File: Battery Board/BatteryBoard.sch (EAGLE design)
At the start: 19 parts, among them IC1 MCP73831T-2ATI_OT, IC2 STM809TWX6F, J0 1725656, U0 STM32L031K4U6, U1 IAUC60N04S6L030HATMA1

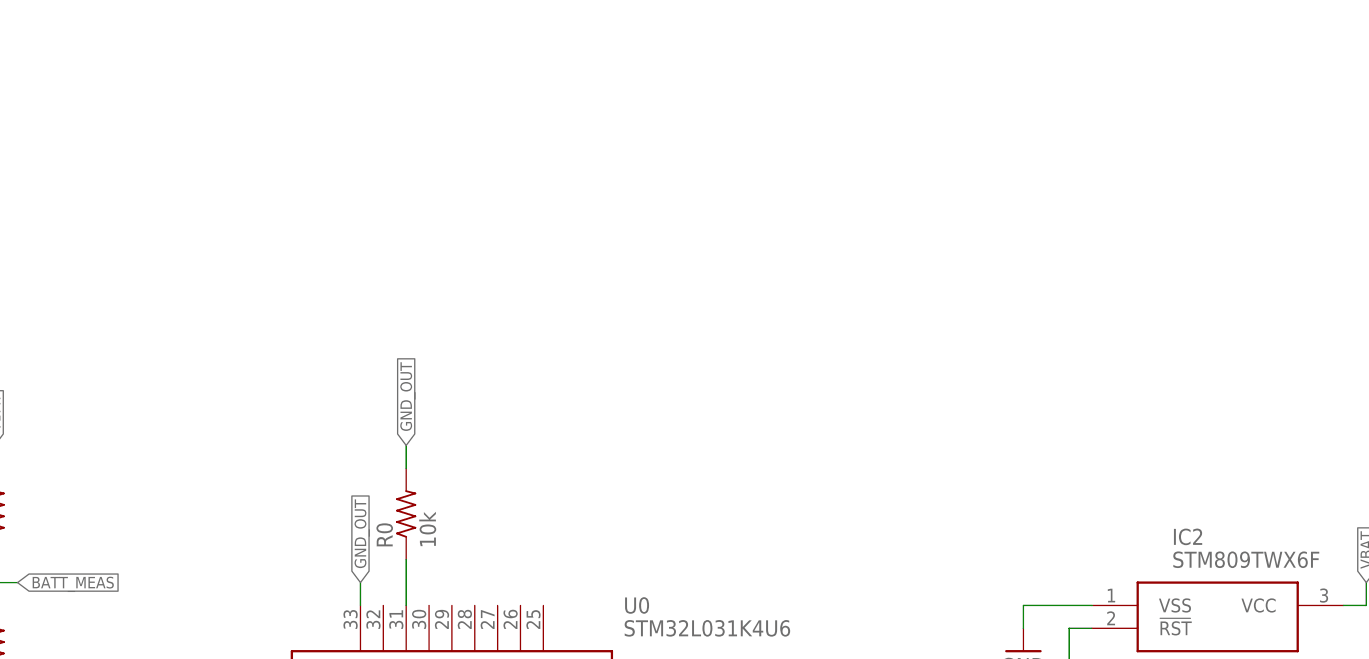
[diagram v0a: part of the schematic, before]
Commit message: Buck Converter Obtained (Switching frequency not)
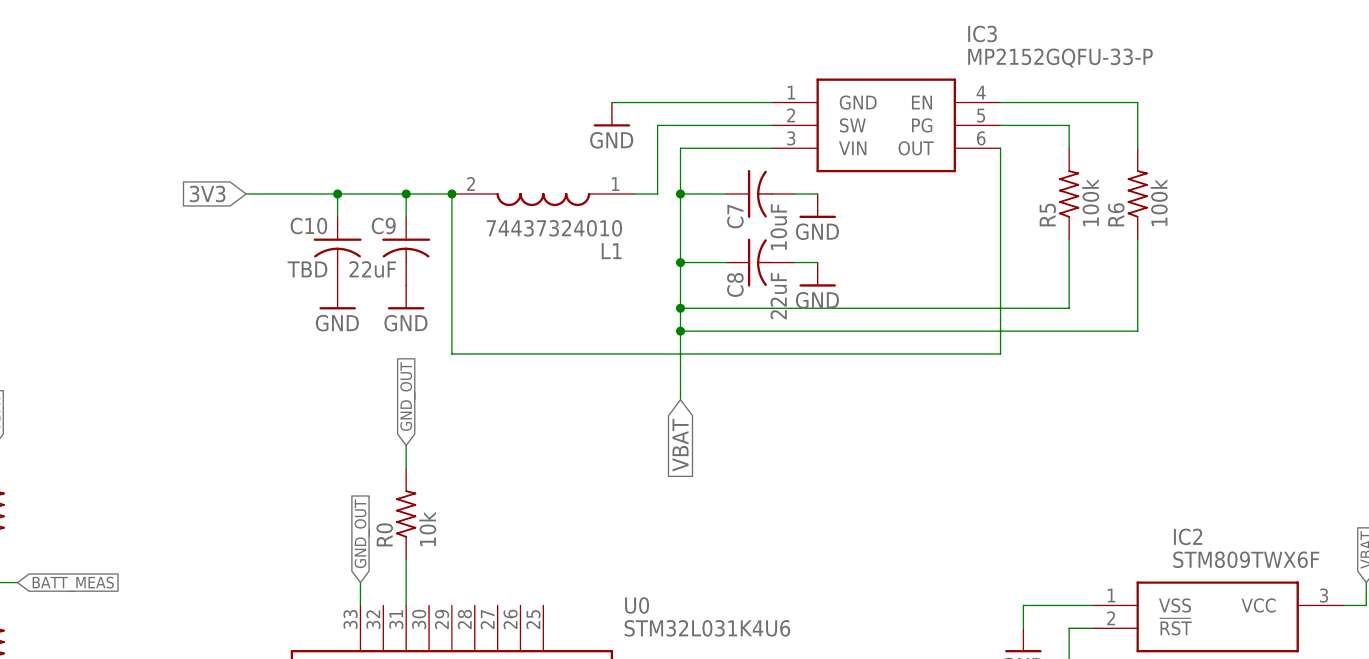
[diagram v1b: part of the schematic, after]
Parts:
- added C10: TBD, rcl:C-USC0805
- added C7: 10uF, rcl:C-USC0805
- added C8, C9: 22uF, rcl:C-USC0805
- added IC3: MP2152GQFU-33-P, SamacSys_Parts:MP2152GQFU-33-P
- added L1: 74437324010, SamacSys_Parts:74437324010
- added R5, R6: 100k, rcl:R-US_R0805
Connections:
- new net N$5: IC3.PG, R5.2
- new net N$6: IC3.EN, R6.2
- new net N$7: IC3.SW, L1.1
- net 3V3: now also C10.1, C9.1, IC3.OUT, L1.2
- net GND: now also C10.2, C7.2, C8.2, C9.2, IC3.GND
- net VBAT: now also C7.1, C8.1, IC3.VIN, R5.1, R6.1
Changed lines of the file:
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@@
 <part name="GND11" library="supply1" library_urn="urn:adsk.eagle:library:371" deviceset="GND" device=""/>
 <part name="U1" library="MarkParts" deviceset="IAUC60N04S6L030HATMA1" device=""/>
+<part name="IC3" library="SamacSys_Parts" deviceset="MP2152GQFU-33-P" device=""/>
+<part name="GND1" library="supply1" library_urn="urn:adsk.eagle:library:371" deviceset="GND" device=""/>
+<part name="R5" library="rcl" library_urn="urn:adsk.eagle:library:334" deviceset="R-US_" device="R0805" package3d_urn="urn:adsk.eagle:package:23553/2" value="100k"/>
+<part name="R6" library="rcl" library_urn="urn:adsk.eagle:library:334" deviceset="R-US_" device="R0805" package3d_urn="urn:adsk.eagle:package:23553/2" value="100k"/>
+<part name="C7" library="rcl" library_urn="urn:adsk.eagle:library:334" deviceset="C-US" device="C0805" package3d_urn="urn:adsk.eagle:package:23617/2" value="10uF"/>
+<part name="C8" library="rcl" library_urn="urn:adsk.eagle:library:334" deviceset="C-US" device="C0805" package3d_urn="urn:adsk.eagle:package:23617/2" value="22uF"/>
+<part name="GND4" library="supply1" library_urn="urn:adsk.eagle:library:371" deviceset="GND" device=""/>
+<part name="GND13" library="supply1" library_urn="urn:adsk.eagle:library:371" deviceset="GND" device=""/>
+<part name="L1" library="SamacSys_Parts" deviceset="74437324010" device=""/>
+<part name="C9" library="rcl" library_urn="urn:adsk.eagle:library:334" deviceset="C-US" device="C0805" package3d_urn="urn:adsk.eagle:package:23617/2" value="22uF"/>
+<part name="C10" library="rcl" library_urn="urn:adsk.eagle:library:334" deviceset="C-US" device="C0805" package3d_urn="urn:adsk.eagle:package:23617/2" value="TBD"/>
+<part name="GND14" library="supply1" library_urn="urn:adsk.eagle:library:371" deviceset="GND" device=""/>
+<part name="GND15" library="supply1" library_urn="urn:adsk.eagle:library:371" deviceset="GND" device=""/>
 </parts>
 <sheets>
@@
 <attribute name="VALUE" x="131.8006" y="57.3786" size="2.0828" layer="96" ratio="6" rot="SR0"/>
 </instance>
+<instance part="IC3" gate="G$1" x="73.66" y="124.46" smashed="yes">
+<attribute name="NAME" x="95.25" y="132.08" size="1.778" layer="95" align="center-left"/>
+<attribute name="VALUE" x="95.25" y="129.54" size="1.778" layer="96" align="center-left"/>
+</instance>
+<instance part="GND1" gate="1" x="55.88" y="121.92" smashed="yes">
+<attribute name="VALUE" x="53.34" y="119.38" size="1.778" layer="96"/>
+</instance>
+<instance part="R5" gate="G$1" x="106.68" y="114.3" smashed="yes" rot="R90">
+<attribute name="NAME" x="105.1814" y="110.49" size="1.778" layer="95" rot="R90"/>
+<attribute name="VALUE" x="109.982" y="110.49" size="1.778" layer="96" rot="R90"/>
+</instance>
+<instance part="R6" gate="G$1" x="114.3" y="114.3" smashed="yes" rot="R90">
+<attribute name="NAME" x="112.8014" y="110.49" size="1.778" layer="95" rot="R90"/>
+<attribute name="VALUE" x="117.602" y="110.49" size="1.778" layer="96" rot="R90"/>
+</instance>
+<instance part="C7" gate="G$1" x="71.12" y="114.3" smashed="yes" rot="MR270">
+<attribute name="NAME" x="70.485" y="113.284" size="1.778" layer="95" rot="MR270"/>
+<attribute name="VALUE" x="75.311" y="113.284" size="1.778" layer="96" rot="MR270"/>
+</instance>
+<instance part="C8" gate="G$1" x="71.12" y="106.68" smashed="yes" rot="MR270">
+<attribute name="NAME" x="70.485" y="105.664" size="1.778" layer="95" rot="MR270"/>
+<attribute name="VALUE" x="75.311" y="105.664" size="1.778" layer="96" rot="MR270"/>
+</instance>
+<instance part="GND4" gate="1" x="78.74" y="111.76" smashed="yes">
+<attribute name="VALUE" x="76.2" y="109.22" size="1.778" layer="96"/>
+</instance>
+<instance part="GND13" gate="1" x="78.74" y="104.14" smashed="yes">
+<attribute name="VALUE" x="76.2" y="101.6" size="1.778" layer="96"/>
+</instance>
+<instance part="L1" gate="G$1" x="58.42" y="114.3" smashed="yes" rot="R180">
+<attribute name="NAME" x="57.15" y="107.95" size="1.778" layer="95" rot="R180" align="center-left"/>
+<attribute name="VALUE" x="57.15" y="110.49" size="1.778" layer="96" rot="R180" align="center-left"/>
+</instance>
+<instance part="C9" gate="G$1" x="33.02" y="109.22" smashed="yes" rot="MR0">
+<attribute name="NAME" x="32.004" y="109.855" size="1.778" layer="95" rot="MR0"/>
+<attribute name="VALUE" x="32.004" y="105.029" size="1.778" layer="96" rot="MR0"/>
+</instance>
+<instance part="C10" gate="G$1" x="25.4" y="109.22" smashed="yes" rot="MR0">
+<attribute name="NAME" x="24.384" y="109.855" size="1.778" layer="95" rot="MR0"/>
+<attribute name="VALUE" x="24.384" y="105.029" size="1.778" layer="96" rot="MR0"/>
+</instance>
+<instance part="GND14" gate="1" x="33.02" y="101.6" smashed="yes">
+<attribute name="VALUE" x="30.48" y="99.06" size="1.778" layer="96"/>
+</instance>
+<instance part="GND15" gate="1" x="25.4" y="101.6" smashed="yes">
+<attribute name="VALUE" x="22.86" y="99.06" size="1.778" layer="96"/>
+</instance>
 </instances>
 <busses>
@@
 <pinref part="GND11" gate="1" pin="GND"/>
 <wire x1="109.22" y1="48.26" x2="109.22" y2="45.72" width="0.1524" layer="91"/>
+</segment>
+<segment>
+<pinref part="IC3" gate="G$1" pin="GND"/>
+<wire x1="73.66" y1="124.46" x2="55.88" y2="124.46" width="0.1524" layer="91"/>
+<pinref part="GND1" gate="1" pin="GND"/>
+</segment>
+<segment>
+<pinref part="C8" gate="G$1" pin="2"/>
+<pinref part="GND13" gate="1" pin="GND"/>
+<wire x1="76.2" y1="106.68" x2="78.74" y2="106.68" width="0.1524" layer="91"/>
+</segment>
+<segment>
+<pinref part="C7" gate="G$1" pin="2"/>
+<pinref part="GND4" gate="1" pin="GND"/>
+<wire x1="76.2" y1="114.3" x2="78.74" y2="114.3" width="0.1524" layer="91"/>
+</segment>
+<segment>
+<pinref part="C9" gate="G$1" pin="2"/>
+<pinref part="GND14" gate="1" pin="GND"/>
+</segment>
+<segment>
+<pinref part="C10" gate="G$1" pin="2"/>
+<pinref part="GND15" gate="1" pin="GND"/>
 </segment>
 </net>
@@
 <wire x1="139.7" y1="68.58" x2="139.7" y2="71.12" width="0.1524" layer="91"/>
 <label x="139.7" y="71.12" size="1.27" layer="95" rot="R90" xref="yes"/>
+</segment>
+<segment>
+<pinref part="IC3" gate="G$1" pin="VIN"/>
+<wire x1="73.66" y1="119.38" x2="63.5" y2="119.38" width="0.1524" layer="91"/>
+<wire x1="63.5" y1="119.38" x2="63.5" y2="114.3" width="0.1524" layer="91"/>
+<wire x1="63.5" y1="114.3" x2="63.5" y2="106.68" width="0.1524" layer="91"/>
+<wire x1="63.5" y1="106.68" x2="63.5" y2="101.6" width="0.1524" layer="91"/>
+<wire x1="63.5" y1="101.6" x2="106.68" y2="101.6" width="0.1524" layer="91"/>
+<junction x="63.5" y="101.6"/>
+<wire x1="106.68" y1="101.6" x2="106.68" y2="109.22" width="0.1524" layer="91"/>
+<pinref part="R5" gate="G$1" pin="1"/>
+<wire x1="63.5" y1="101.6" x2="63.5" y2="99.06" width="0.1524" layer="91"/>
+<wire x1="63.5" y1="99.06" x2="114.3" y2="99.06" width="0.1524" layer="91"/>
+<wire x1="114.3" y1="99.06" x2="114.3" y2="109.22" width="0.1524" layer="91"/>
+<pinref part="R6" gate="G$1" pin="1"/>
+<wire x1="63.5" y1="99.06" x2="63.5" y2="91.44" width="0.1524" layer="91"/>
+<junction x="63.5" y="99.06"/>
+<label x="63.5" y="91.44" size="1.778" layer="95" rot="R270" xref="yes"/>
+<pinref part="C8" gate="G$1" pin="1"/>
+<wire x1="63.5" y1="106.68" x2="68.58" y2="106.68" width="0.1524" layer="91"/>
+<junction x="63.5" y="106.68"/>
+<pinref part="C7" gate="G$1" pin="1"/>
+<wire x1="63.5" y1="114.3" x2="68.58" y2="114.3" width="0.1524" layer="91"/>
+<junction x="63.5" y="114.3"/>
 </segment>
 </net>
@@
 <label x="63.5" y="33.02" size="1.27" layer="95" xref="yes"/>
 </segment>
-</net>
+<segment>
+<pinref part="L1" gate="G$1" pin="2"/>
+<pinref part="IC3" gate="G$1" pin="OUT"/>
+<wire x1="99.06" y1="119.38" x2="99.06" y2="96.52" width="0.1524" layer="91"/>
+<wire x1="99.06" y1="96.52" x2="38.1" y2="96.52" width="0.1524" layer="91"/>
+<wire x1="38.1" y1="96.52" x2="38.1" y2="114.3" width="0.1524" layer="91"/>
+<junction x="38.1" y="114.3"/>
+<wire x1="38.1" y1="114.3" x2="33.02" y2="114.3" width="0.1524" layer="91"/>
+<pinref part="C10" gate="G$1" pin="1"/>
+<wire x1="33.02" y1="114.3" x2="25.4" y2="114.3" width="0.1524" layer="91"/>
+<wire x1="25.4" y1="114.3" x2="25.4" y2="111.76" width="0.1524" layer="91"/>
+<pinref part="C9" gate="G$1" pin="1"/>
+<wire x1="33.02" y1="114.3" x2="33.02" y2="111.76" width="0.1524" layer="91"/>
+<junction x="33.02" y="114.3"/>
+<wire x1="25.4" y1="114.3" x2="15.24" y2="114.3" width="0.1524" layer="91"/>
+<junction x="25.4" y="114.3"/>
+<label x="15.24" y="114.3" size="1.778" layer="95" rot="R180" xref="yes"/>
+</segment>
+</net>
+<net name="N$5" class="0">
+<segment>
+<pinref part="R5" gate="G$1" pin="2"/>
+<pinref part="IC3" gate="G$1" pin="PG"/>
+<wire x1="106.68" y1="119.38" x2="106.68" y2="121.92" width="0.1524" layer="91"/>
+<wire x1="106.68" y1="121.92" x2="99.06" y2="121.92" width="0.1524" layer="91"/>
+</segment>
+</net>
+<net name="N$6" class="0">
+<segment>
+<pinref part="R6" gate="G$1" pin="2"/>
+<wire x1="114.3" y1="119.38" x2="114.3" y2="124.46" width="0.1524" layer="91"/>
+<pinref part="IC3" gate="G$1" pin="EN"/>
+<wire x1="114.3" y1="124.46" x2="99.06" y2="124.46" width="0.1524" layer="91"/>
+</segment>
+</net>
+<net name="N$7" class="0">
+<segment>
+<pinref part="IC3" gate="G$1" pin="SW"/>
+<wire x1="73.66" y1="121.92" x2="60.96" y2="121.92" width="0.1524" layer="91"/>
+<wire x1="60.96" y1="121.92" x2="60.96" y2="114.3" width="0.1524" layer="91"/>
+<wire x1="60.96" y1="114.3" x2="58.42" y2="114.3" width="0.1524" layer="91"/>
+<pinref part="L1" gate="G$1" pin="1"/>
+</segment>
+</net>

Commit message: started the pcb
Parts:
- removed IC1: MCP73831T-2ATI_OT, SamacSys_Parts:MCP73831T-2ATI_OT
- added Q1: IAUC60N04S6L030HATMA1, MarkParts:IAUC60N04S6L030HATMA1
- U1: value IAUC60N04S6L030HATMA1 -> MCP73831T-2ATI_OT; device MarkParts:IAUC60N04S6L030HATMA1 -> SamacSys_Parts:MCP73831T-2ATI_OT
- renumbered IC2 to U3, IC3 to U2
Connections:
- net N$1 renamed BOOT0
- net N$7 renamed L1-SW
- net GND: now also Q1.PHASE_2, U1.VSS; no longer IC1.VSS, U1.PHASE_2
- net GND_OUT: now also Q1.BATTERY; no longer U1.BATTERY
- net N$4: now also U1.PROG; no longer IC1.PROG
- net PROTECTION_NRST: now also Q1.G_2; no longer U1.G_2
- net STAT: now also U1.STAT; no longer IC1.STAT
- net VBAT: now also U1.VBAT; no longer IC1.VBAT
- net VUSB: now also U1.VDD; no longer IC1.VDD
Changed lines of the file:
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@@
 <part name="J0" library="SamacSys_Parts" deviceset="1725656" device=""/>
 <part name="GND6" library="supply1" library_urn="urn:adsk.eagle:library:371" deviceset="GND" device=""/>
-<part name="IC1" library="SamacSys_Parts" deviceset="MCP73831T-2ATI_OT" device=""/>
+<part name="U1" library="SamacSys_Parts" deviceset="MCP73831T-2ATI_OT" device=""/>
 <part name="C5" library="rcl" library_urn="urn:adsk.eagle:library:334" deviceset="C-US" device="C0805" package3d_urn="urn:adsk.eagle:package:23617/2" value="4.7uF"/>
 <part name="GND7" library="supply1" library_urn="urn:adsk.eagle:library:371" deviceset="GND" device=""/>
@@
 <part name="C6" library="rcl" library_urn="urn:adsk.eagle:library:334" deviceset="C-US" device="C0805" package3d_urn="urn:adsk.eagle:package:23617/2" value="4.7uF"/>
 <part name="GND10" library="supply1" library_urn="urn:adsk.eagle:library:371" deviceset="GND" device=""/>
-<part name="IC2" library="SamacSys_Parts" deviceset="STM809TWX6F" device=""/>
+<part name="U3" library="SamacSys_Parts" deviceset="STM809TWX6F" device=""/>
 <part name="GND12" library="supply1" library_urn="urn:adsk.eagle:library:371" deviceset="GND" device=""/>
 <part name="GND11" library="supply1" library_urn="urn:adsk.eagle:library:371" deviceset="GND" device=""/>
-<part name="U1" library="MarkParts" deviceset="IAUC60N04S6L030HATMA1" device=""/>
-<part name="IC3" library="SamacSys_Parts" deviceset="MP2152GQFU-33-P" device=""/>
+<part name="Q1" library="MarkParts" deviceset="IAUC60N04S6L030HATMA1" device=""/>
+<part name="U2" library="SamacSys_Parts" deviceset="MP2152GQFU-33-P" device=""/>
 <part name="GND1" library="supply1" library_urn="urn:adsk.eagle:library:371" deviceset="GND" device=""/>
 <part name="R5" library="rcl" library_urn="urn:adsk.eagle:library:334" deviceset="R-US_" device="R0805" package3d_urn="urn:adsk.eagle:package:23553/2" value="100k"/>
@@
 <attribute name="VALUE" x="-53.34" y="76.2" size="1.778" layer="96" rot="R270"/>
 </instance>
-<instance part="IC1" gate="G$1" x="78.74" y="7.62" smashed="yes">
+<instance part="U1" gate="G$1" x="78.74" y="7.62" smashed="yes">
 <attribute name="NAME" x="102.87" y="15.24" size="1.778" layer="95" align="center-left"/>
 <attribute name="VALUE" x="102.87" y="12.7" size="1.778" layer="96" align="center-left"/>
@@
 <attribute name="VALUE" x="129.54" y="-5.08" size="1.778" layer="96"/>
 </instance>
-<instance part="IC2" gate="G$1" x="109.22" y="68.58" smashed="yes">
+<instance part="U3" gate="G$1" x="109.22" y="68.58" smashed="yes">
 <attribute name="NAME" x="118.11" y="76.2" size="1.778" layer="95" align="center-left"/>
 <attribute name="VALUE" x="118.11" y="73.66" size="1.778" layer="96" align="center-left"/>
@@
 <attribute name="VALUE" x="106.68" y="40.64" size="1.778" layer="96"/>
 </instance>
-<instance part="U1" gate="A" x="111.76" y="50.8" smashed="yes">
+<instance part="Q1" gate="A" x="111.76" y="50.8" smashed="yes">
 <attribute name="NAME" x="132.4356" y="59.9186" size="2.0828" layer="95" ratio="6" rot="SR0"/>
 <attribute name="VALUE" x="131.8006" y="57.3786" size="2.0828" layer="96" ratio="6" rot="SR0"/>
 </instance>
-<instance part="IC3" gate="G$1" x="73.66" y="124.46" smashed="yes">
+<instance part="U2" gate="G$1" x="73.66" y="124.46" smashed="yes">
 <attribute name="NAME" x="95.25" y="132.08" size="1.778" layer="95" align="center-left"/>
 <attribute name="VALUE" x="95.25" y="129.54" size="1.778" layer="96" align="center-left"/>
@@
 </busses>
 <nets>
-<net name="N$1" class="0">
+<net name="BOOT0" class="0">
 <segment>
 <pinref part="U0" gate="G$1" pin="BOOT0"/>
@@
 </segment>
 <segment>
-<pinref part="IC1" gate="G$1" pin="VSS"/>
+<pinref part="U1" gate="G$1" pin="VSS"/>
 <wire x1="78.74" y1="5.08" x2="76.2" y2="5.08" width="0.1524" layer="91"/>
 <pinref part="GND8" gate="1" pin="GND"/>
@@
 </segment>
 <segment>
-<pinref part="IC2" gate="G$1" pin="VSS"/>
+<pinref part="U3" gate="G$1" pin="VSS"/>
 <wire x1="109.22" y1="68.58" x2="101.6" y2="68.58" width="0.1524" layer="91"/>
 <wire x1="101.6" y1="68.58" x2="101.6" y2="66.04" width="0.1524" layer="91"/>
@@
 </segment>
 <segment>
-<pinref part="U1" gate="A" pin="PHASE_2"/>
+<pinref part="Q1" gate="A" pin="PHASE_2"/>
 <wire x1="114.3" y1="48.26" x2="109.22" y2="48.26" width="0.1524" layer="91"/>
 <pinref part="GND11" gate="1" pin="GND"/>
@@
 </segment>
 <segment>
-<pinref part="IC3" gate="G$1" pin="GND"/>
+<pinref part="U2" gate="G$1" pin="GND"/>
 <wire x1="73.66" y1="124.46" x2="55.88" y2="124.46" width="0.1524" layer="91"/>
 <pinref part="GND1" gate="1" pin="GND"/>
@@
 </segment>
 <segment>
-<pinref part="IC1" gate="G$1" pin="VBAT"/>
+<pinref part="U1" gate="G$1" pin="VBAT"/>
 <wire x1="78.74" y1="2.54" x2="78.74" y2="-5.08" width="0.1524" layer="91"/>
 <wire x1="78.74" y1="-5.08" x2="124.46" y2="-5.08" width="0.1524" layer="91"/>
@@
 </segment>
 <segment>
-<pinref part="IC2" gate="G$1" pin="VCC"/>
+<pinref part="U3" gate="G$1" pin="VCC"/>
 <wire x1="139.7" y1="68.58" x2="137.16" y2="68.58" width="0.1524" layer="91"/>
 <wire x1="139.7" y1="68.58" x2="139.7" y2="71.12" width="0.1524" layer="91"/>
@@
 </segment>
 <segment>
-<pinref part="IC3" gate="G$1" pin="VIN"/>
+<pinref part="U2" gate="G$1" pin="VIN"/>
 <wire x1="73.66" y1="119.38" x2="63.5" y2="119.38" width="0.1524" layer="91"/>
 <wire x1="63.5" y1="119.38" x2="63.5" y2="114.3" width="0.1524" layer="91"/>
@@
 <net name="VUSB" class="0">
 <segment>
-<pinref part="IC1" gate="G$1" pin="VDD"/>
+<pinref part="U1" gate="G$1" pin="VDD"/>
 <wire x1="106.68" y1="7.62" x2="106.68" y2="12.7" width="0.1524" layer="91"/>
 <wire x1="106.68" y1="12.7" x2="55.88" y2="12.7" width="0.1524" layer="91"/>
@@
 <net name="N$4" class="0">
 <segment>
-<pinref part="IC1" gate="G$1" pin="PROG"/>
+<pinref part="U1" gate="G$1" pin="PROG"/>
 <wire x1="106.68" y1="5.08" x2="109.22" y2="5.08" width="0.1524" layer="91"/>
 <pinref part="R4" gate="G$1" pin="2"/>
@@
 <wire x1="55.88" y1="-12.7" x2="68.58" y2="-12.7" width="0.1524" layer="91"/>
 <wire x1="68.58" y1="-12.7" x2="68.58" y2="7.62" width="0.1524" layer="91"/>
-<pinref part="IC1" gate="G$1" pin="STAT"/>
+<pinref part="U1" gate="G$1" pin="STAT"/>
 <wire x1="68.58" y1="7.62" x2="78.74" y2="7.62" width="0.1524" layer="91"/>
 <label x="68.58" y="7.62" size="1.27" layer="95" rot="R180" xref="yes"/>
@@
 <net name="PROTECTION_NRST" class="0">
 <segment>
-<pinref part="IC2" gate="G$1" pin="!RST"/>
+<pinref part="U3" gate="G$1" pin="!RST"/>
 <wire x1="109.22" y1="66.04" x2="106.68" y2="66.04" width="0.1524" layer="91"/>
 <wire x1="106.68" y1="50.8" x2="106.68" y2="66.04" width="0.1524" layer="91"/>
-<pinref part="U1" gate="A" pin="G_2"/>
+<pinref part="Q1" gate="A" pin="G_2"/>
 <wire x1="106.68" y1="50.8" x2="114.3" y2="50.8" width="0.1524" layer="91"/>
 </segment>
@@
 </segment>
 <segment>
-<pinref part="U1" gate="A" pin="BATTERY"/>
+<pinref part="Q1" gate="A" pin="BATTERY"/>
 <wire x1="160.02" y1="50.8" x2="162.56" y2="50.8" width="0.1524" layer="91"/>
 <label x="162.56" y="50.8" size="1.27" layer="95" xref="yes"/>
@@
 <segment>
 <pinref part="L1" gate="G$1" pin="2"/>
-<pinref part="IC3" gate="G$1" pin="OUT"/>
+<pinref part="U2" gate="G$1" pin="OUT"/>
 <wire x1="99.06" y1="119.38" x2="99.06" y2="96.52" width="0.1524" layer="91"/>
 <wire x1="99.06" y1="96.52" x2="38.1" y2="96.52" width="0.1524" layer="91"/>
@@
 <segment>
 <pinref part="R5" gate="G$1" pin="2"/>
-<pinref part="IC3" gate="G$1" pin="PG"/>
+<pinref part="U2" gate="G$1" pin="PG"/>
 <wire x1="106.68" y1="119.38" x2="106.68" y2="121.92" width="0.1524" layer="91"/>
 <wire x1="106.68" y1="121.92" x2="99.06" y2="121.92" width="0.1524" layer="91"/>
@@
 <pinref part="R6" gate="G$1" pin="2"/>
 <wire x1="114.3" y1="119.38" x2="114.3" y2="124.46" width="0.1524" layer="91"/>
-<pinref part="IC3" gate="G$1" pin="EN"/>
+<pinref part="U2" gate="G$1" pin="EN"/>
 <wire x1="114.3" y1="124.46" x2="99.06" y2="124.46" width="0.1524" layer="91"/>
 </segment>
 </net>
-<net name="N$7" class="0">
-<segment>
-<pinref part="IC3" gate="G$1" pin="SW"/>
+<net name="L1-SW" class="0">
+<segment>
+<pinref part="U2" gate="G$1" pin="SW"/>
 <wire x1="73.66" y1="121.92" x2="60.96" y2="121.92" width="0.1524" layer="91"/>
 <wire x1="60.96" y1="121.92" x2="60.96" y2="114.3" width="0.1524" layer="91"/>
